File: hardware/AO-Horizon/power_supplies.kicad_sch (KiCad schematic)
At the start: 28 parts

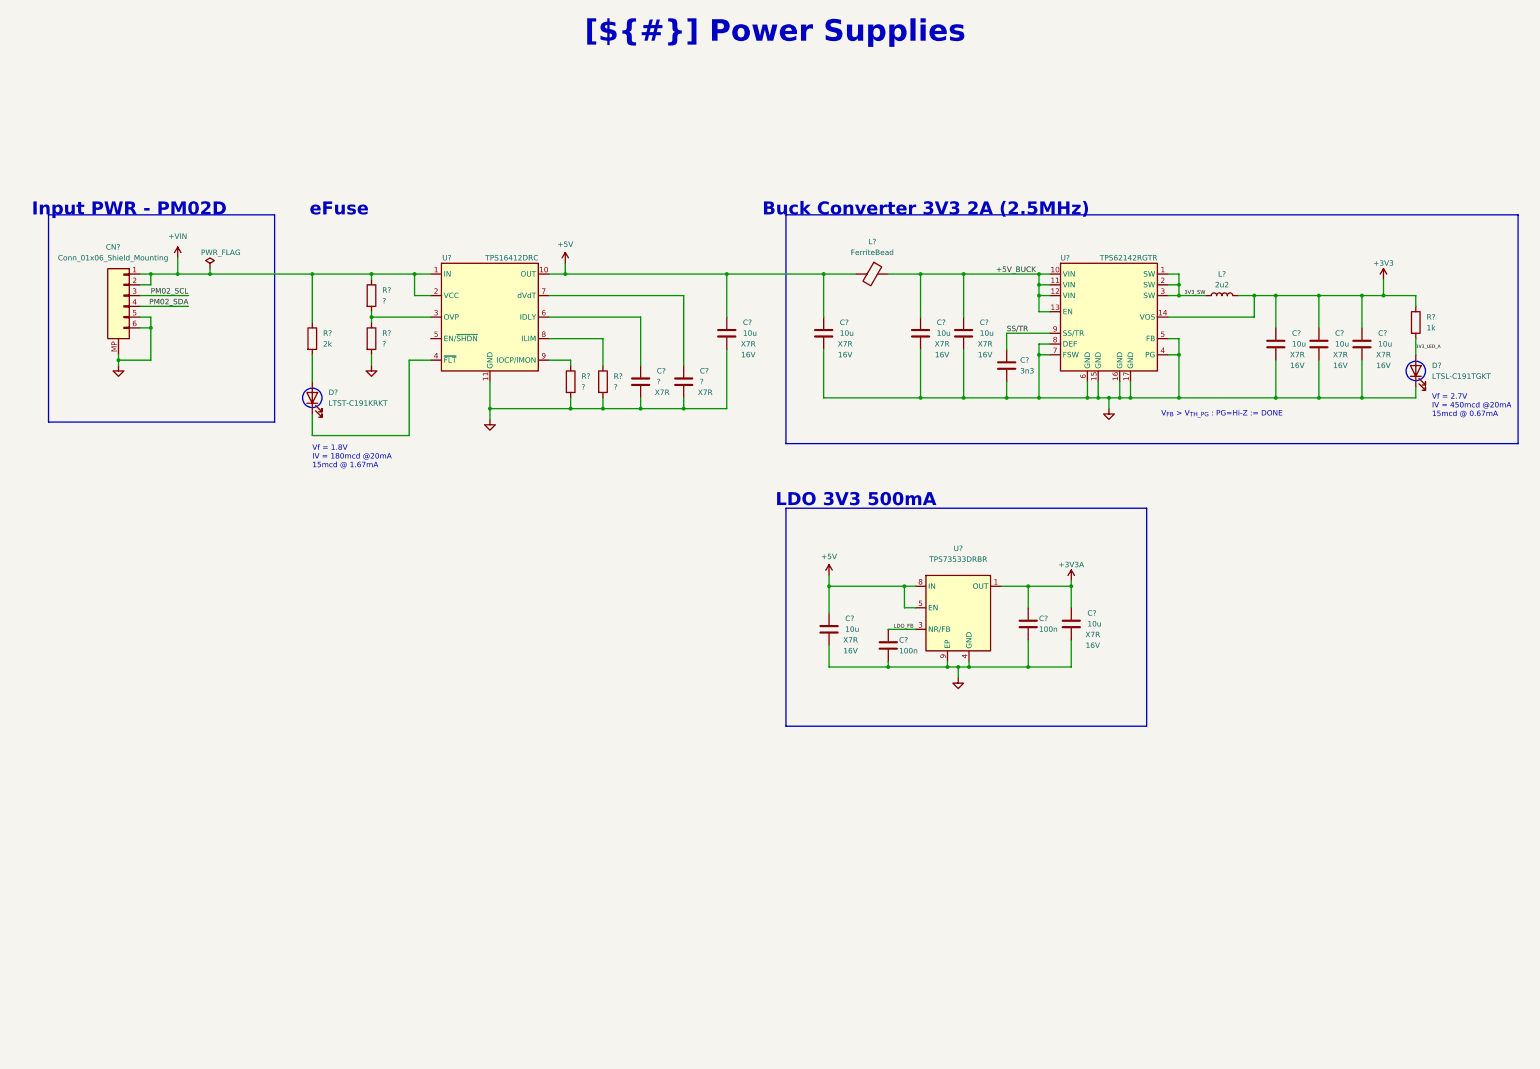
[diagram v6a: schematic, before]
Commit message: feat: TPS259251DRC eFuse (DEC-026), spec 0.18 and power view update (#30)
* docs(readme): simplify workflow diagram explanation

Mark DRAFT as under review, sync CHECK label, and add a colour key in README and template.

Co-Authored-By: Claude Sonnet 5.5 <noreply@anthropic.com>

* Update settings.json

* change spec file name

* update git-workflow skill

* change skill name by add hw-*

* docs: update AeroOptix-Horizon hardware spec

* docs: consolidate hardware handoff into checklist

* Update CLAUDE.md

* Update CLAUDE.md

* Update CLAUDE.md

* feat(hooks): replace protect hook with rule-based v2

Move file-protection rules into hooks/protect.json (allow > deny > ask)
and use ask for editable-with-approval files instead of a hard block.
Bash/PowerShell checks now inspect write targets, not any mention of a
protected path. Align settings.json permissions and drop the old hook.

Co-Authored-By: Claude Sonnet 5.5 <noreply@anthropic.com>

* docs: update CLAUDE.md for protection tiers and skill names

Describe the ask/deny protection rules, the v2 hook and protect.json,
and fix stale skill and template names.

Co-Authored-By: Claude Sonnet 5.5 <noreply@anthropic.com>

* Update .gitignore

* Update .gitignore

* Update .gitignore

* del skills

* Update engineering.md

* Update git-workflow.md

* Update hardware-workflow.md

* Update settings.json

* Update pull_request_template.md

* Update .gitignore

* Update .gitignore

* Delete SKILL.md

* Delete SKILL.md

* Update .gitignore

* add git-workflow skill

* Update CLAUDE.md

* Update protect.json

* Update settings.json

* Create MEMORY.md

* feat(agents): add codex-hw-delegate for bounded Codex tasks

Add a project agent that delegates one small, read-only-by-default task
to Codex CLI. It gates trivial or ambiguous requests, refuses PDF and
KiCad file contents, never mutates git, cross-checks Codex output and
returns a fixed report format.

Co-Authored-By: Claude Sonnet 5.5 <noreply@anthropic.com>

* fix(hooks): res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
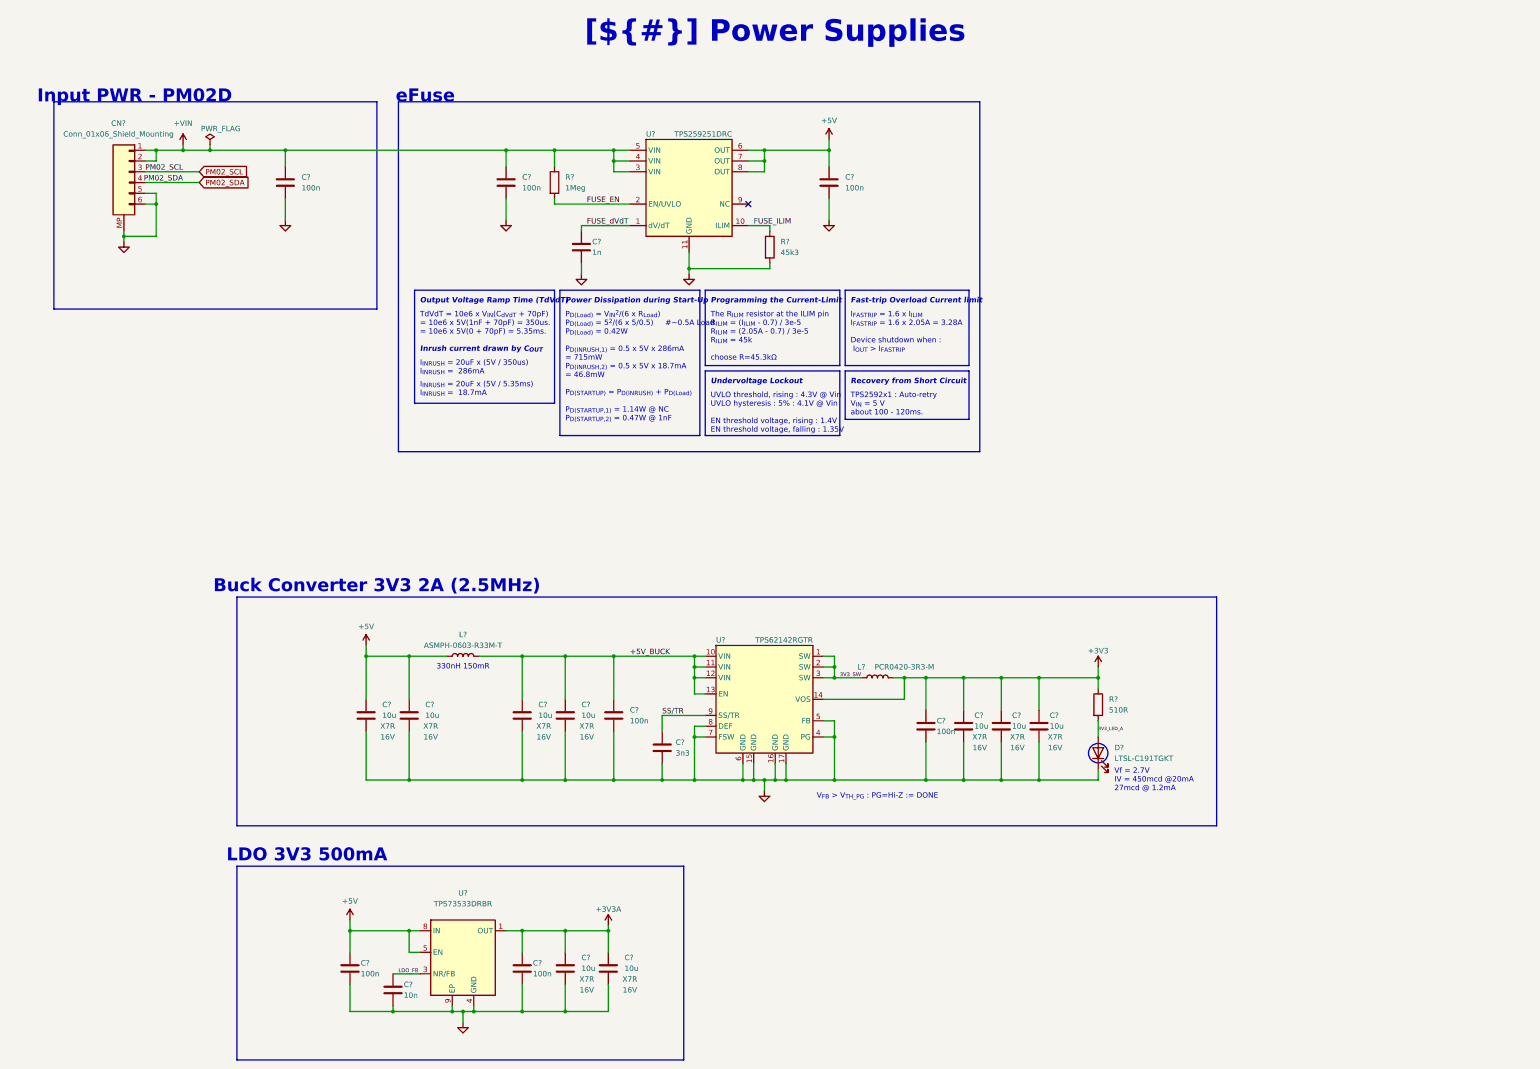
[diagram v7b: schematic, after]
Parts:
- removed C? (x2): 100n, 0_Capacitor_SMD:C_0603_1608Metric_NomDensity, symbol Device:C
- removed C? (x8): 10u, 0_Capacitor_SMD:C_0805_2012Metric_NomDensity, symbol Device:C
- removed C? (x2): ?, symbol Device:C
- removed D?: LTST-C191KRKT, 0_LED_SMD:LED_0603_1608Metric, symbol Device:LED
- removed L?: FerriteBead, symbol Device:FerriteBead
- removed R?: 1k, 0_Resistor_SMD:R_0603_1608Metric_NomDensity, symbol Device:R
- removed R? (x4): ?, 0_Resistor_SMD:R_0603_1608Metric_NomDensity, symbol Device:R
- removed R?: 2k, 0_Resistor_SMD:R_0603_1608Metric_NomDensity, symbol Device:R
- removed U?: TPS16412DRC, 0_Package_SON:Texas_VSON-10-1EP_3x3mm_P0.5mm_EP1.65x2.4mm_ThermalVias, symbol 0_Protection_eFuse:TPS16412DRC
- added C? (x8): 10u, 0_Capacitor_SMD:C_0805_2012Metric_NomDensity, symbol Device:C
- added C? (x7): 100n, 0_Capacitor_SMD:C_0402_1005Metric_NomDensity, symbol Device:C
- added C?: 10n, symbol Device:C
- added C?: 1n, symbol Device:C
- added L?: ASMPH-0603-R33M-T, 0_Inductor_SMD:L_0603_1608Metric, symbol Device:L
- added R?: 1Meg, symbol Device:R
- added R?: 510R, symbol Device:R
- added R?: 45k3, symbol Device:R
- added U?: TPS259251DRC, 0_Package_SON:Texas_VSON-10-1EP_3x3mm_P0.5mm_EP1.65x2.4mm_ThermalVias, symbol 0_Protection_eFuse:TPS25925xDRC
- C?: MFR.P/N (none) -> GRM1885C1H332JA01D; MPN GRM1885C1H332JA01D -> (none)
- C?: MFR.P/N (none) -> GRM21BZ71C106KE15L; MPN GRM21BZ71C106KE15L -> (none)
- L?: value 2u2 -> PCR0420-3R3-M; footprint 0_Inductor_SMD:L_Abracon_AOTA-B252010S -> 0_Inductor_SMD:L_JIERR_PCR0420; LCSC C19271752 -> C53896857; MFR ABRACON -> JIERR; MFR.P/N (none) -> PCR0420-3R3-M; MPN AOTA-B252010S2R2MT -> (none)
- U?: MFR.P/N (none) -> TPS73533DRBR; MPN TPS73533DRBR -> (none)
- U?: MFR.P/N (none) -> TPS62142RGTR; MPN TPS62142RGTR -> (none)
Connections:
- net +3V3: now also C?.1, C?.1, C?.1, C?.1, R?.1
- net +3V3A: now also C?.1, C?.1, C?.1
- net +5V: now also C?.1, C?.1, C?.1, C?.1, L?.1, U?.6 (OUT), U?.7 (OUT), U?.8 (OUT)
- net +5V_BUCK: now also C?.1, C?.1, L?.2
- net +VIN: now also C?.1, C?.1, R?.1, U?.3 (VIN), U?.4 (VIN), U?.5 (VIN)
- net 3V3_LED_A: now also R?.2
- net GND: now also C?.2, C?.2, C?.2, C?.2, C?.2, C?.2, C?.2, C?.2, C?.2, C?.2, C?.2, C?.2, C?.2, C?.2, C?.2, C?.2, C?.2, R?.2, U?.11 (GND)
- net LDO_FB: now also C?.1
- new net FUSE_EN: R?.2, U?.2 (EN/UVLO)
- new net FUSE_ILIM: R?.1, U?.10 (ILIM)
- new net FUSE_dVdT: C?.1, U?.1 (dV/dT)
- no-connect marks 0 -> 1
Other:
- note added: "330nH 150mR"
- note added: "Fast-trip Overload Current limit"
- note added: "I_{FASTRIP} = 1.6 x I_{ILIM} I_{FASTRIP} = 1.6 x 2.05A = 3.28A Device shutdown when : I_{OUT} > I_{FASTRIP}"
- note added: "I_{INRUSH} = 20uF x (5V / 350us) I_{INRUSH} = 286mA"
- note added: "I_{INRUSH} = 20uF x (5V / 5.35ms) I_{INRUSH} = 18.7mA"
- note added: "Inrush current drawn by C_{OUT}"
- note added: "Output Voltage Ramp Time (TdVdT)"
- note added: "P_{D(Load)} = V_{IN}^{2}/(6 x R_{Load}) P_{D(Load)} = 5^{2}/(6 x 5/0.5) #~0.5A Load P_{D(Load)} = 0.42W P_{D(INRUSH,1)} = 0.5 x 5V x 286mA = 715mW P_{D(INRUSH,2)} = 0.5 x 5V x 18.7mA = 46.8mW P_{D(STARTUP)} = P_{D(INRUSH)} + P_{D(Load)} P_{D(STARTUP,1)} = 1.14W @ NC P_{D(STARTUP,2)} = 0.47W @ 1nF"
- note added: "Power Dissipation during Start-Up"
- note added: "Programming the Current-Limit"
- note added: "Recovery from Short Circuit"
- note added: "TPS2592x1 : Auto-retry V_{IN} = 5 V about 100 - 120ms."
- note added: "TdVdT = 10e6 x V_{IN}(C_{dVdT} + 70pF) = 10e6 x 5V(1nF + 70pF) = 350us. = 10e6 x 5V(0 + 70pF) = 5.35ms."
- note added: "The R_{ILIM} resistor at the ILIM pin R_{ILIM} = (I_{ILIM} - 0.7) / 3e-5 R_{ILIM} = (2.05A - 0.7) / 3e-5 R_{ILIM} = 45k choose R=45.3kΩ"
- note added: "UVLO threshold, rising : 4.3V @ Vin UVLO hysteresis : 5% : 4.1V @ Vin EN threshold voltage, rising : 1.4V EN threshold voltage, falling : 1.35V"
- note added: "Undervoltage Lockout"
- note added: "Vf = 2.7V IV = 450mcd @20mA 27mcd @ 1.2mA"
- note removed: "Vf = 1.8V IV = 180mcd @20mA 15mcd @ 1.67mA"
- note removed: "Vf = 2.7V IV = 450mcd @20mA 15mcd @ 0.67mA"
- moved on the sheet: C?, CN?, D?, L?, U?

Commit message: feat: close the power sheet capture (spec 0.19, DEC-027, DEC-028) (#31)
* docs(readme): simplify workflow diagram explanation

Mark DRAFT as under review, sync CHECK label, and add a colour key in README and template.

Co-Authored-By: Claude Sonnet 5.5 <noreply@anthropic.com>

* Update settings.json

* change spec file name

* update git-workflow skill

* change skill name by add hw-*

* docs: update AeroOptix-Horizon hardware spec

* docs: consolidate hardware handoff into checklist

* Update CLAUDE.md

* Update CLAUDE.md

* Update CLAUDE.md

* feat(hooks): replace protect hook with rule-based v2

Move file-protection rules into hooks/protect.json (allow > deny > ask)
and use ask for editable-with-approval files instead of a hard block.
Bash/PowerShell checks now inspect write targets, not any mention of a
protected path. Align settings.json permissions and drop the old hook.

Co-Authored-By: Claude Sonnet 5.5 <noreply@anthropic.com>

* docs: update CLAUDE.md for protection tiers and skill names

Describe the ask/deny protection rules, the v2 hook and protect.json,
and fix stale skill and template names.

Co-Authored-By: Claude Sonnet 5.5 <noreply@anthropic.com>

* Update .gitignore

* Update .gitignore

* Update .gitignore

* del skills

* Update engineering.md

* Update git-workflow.md

* Update hardware-workflow.md

* Update settings.json

* Update pull_request_template.md

* Update .gitignore

* Update .gitignore

* Delete SKILL.md

* Delete SKILL.md

* Update .gitignore

* add git-workflow skill

* Update CLAUDE.md

* Update protect.json

* Update settings.json

* Create MEMORY.md

* feat(agents): add codex-hw-delegate for bounded Codex tasks

Add a project agent that delegates one small, read-only-by-default task
to Codex CLI. It gates trivial or ambiguous requests, refuses PDF and
KiCad file contents, never mutates git, cross-checks Codex output and
returns a fixed report format.

Co-Authored-By: Claude Sonnet 5.5 <noreply@anthropic.com>

* fix(hooks): resol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
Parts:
- removed C?: 100n, 0_Capacitor_SMD:C_0402_1005Metric_NomDensity, symbol Device:C
- removed C?: 10u, 0_Capacitor_SMD:C_0805_2012Metric_NomDensity, symbol Device:C
- added C107, C116: 10u, 0_Capacitor_SMD:C_0805_2012Metric_NomDensity, symbol Device:C
- added C119: 100n, 0_Capacitor_SMD:C_0402_1005Metric_NomDensity, symbol Device:C
- added R103: 100k, 0_Resistor_SMD:R_0402_1005Metric_NomDensity, symbol Device:R
- C103, C118: renamed from C?; footprint (none) -> 0_Capacitor_SMD:C_0402_1005Metric_NomDensity
- C111: renamed from C?; value 3n3 -> 10n; footprint 0_Capacitor_SMD:C_0603_1608Metric_NomDensity -> 0_Capacitor_SMD:C_0402_1005Metric_NomDensity; LCSC C77036 -> (none); MFR.P/N GRM1885C1H332JA01D -> (none)
- R101, R102, R104: renamed from R?; footprint (none) -> 0_Resistor_SMD:R_0402_1005Metric_NomDensity
- gave numbers to parts that had none: 21
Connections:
- net +3V3: now also R103.2
- net +3V3A: now also C119.1
- net +5V: now also C116.1
- net +5V_BUCK: now also C107.1
- net GND: now also C107.2, C116.2, C119.2; no longer U102.4 (PG)
- net +VIN: no longer names the net of C101.1, C102.1, CN101.1 (Pin_1), CN101.2 (Pin_2), R101.1, U101.3 (VIN), U101.4 (VIN), U101.5 (VIN)
- new net 3V3_DONE: R103.1, U102.4 (PG)
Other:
- note added: "At Load 3.3V 1.5A |Z_{IN}(0)| = 2.2Ω"
- note added: "C_{SS} = t_{ss} x (2.5e-6/1.25) t_{ss} = 10e-9 x (1.25/2.5e-6) = 5ms."
- note added: "Conv. Input Impedance"
- note added: "During Start-up : PG = Low When V_{OUT} > V_{TH_PG} : PG = Hi-Z otherwise PG = Hi-z"
- note added: "GRM21BZ71C106KE15L, 10uF 16V Derating 20.5% @ 3.3V C_{OUT} = 0.795 x (3 x 10uF) = 23.85uF"
- note added: "GRM21BZ71C106KE15L, 10uF 16V Derating 39% @ 5.2V C_{OUT} = 0.61 x (3 x 10uF) = 18uF"
- note added: "Input Capacitance"
- note added: "Input Filter Design"
- note added: "L : 3.3uH C : 10uF < C_{OUT} < 100uF The DC bias effect need considered"
- note added: "LC Output Filter Range"
- note added: "Margin below |Z_{IN}(0)| = 20log(2.2/0.189) = 21.3dB"
- note added: "Output Capacitance"
- note added: "Output Impedance"
- note added: "Power Good Pin Logic (TPS6214x)"
- note added: "R = 1/Q x sqrt(L/C) R = 1/1 x sqrt(0.33/18) = ~0.14Ω Choose 0.15Ω DCR Q = 1/0.15 x sqrt(0.33/18) = 0.9"
- note added: "Soft-Start of the V_{OUT}"
- note added: "Z_{MAX} ~ R(1 + Q^{2}/2 - Q^{4}/8) = ~0.198Ω"
- note removed: "V_{FB} > V_{TH_PG} : PG=Hi-Z := DONE"
- moved on the sheet: C105, C106, C108, C109, C110, C111, C112, C113, C114, C115, C117, C118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
